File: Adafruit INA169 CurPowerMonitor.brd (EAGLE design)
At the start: 22.9 x 21 mm, 13 parts, among them U1 INA169

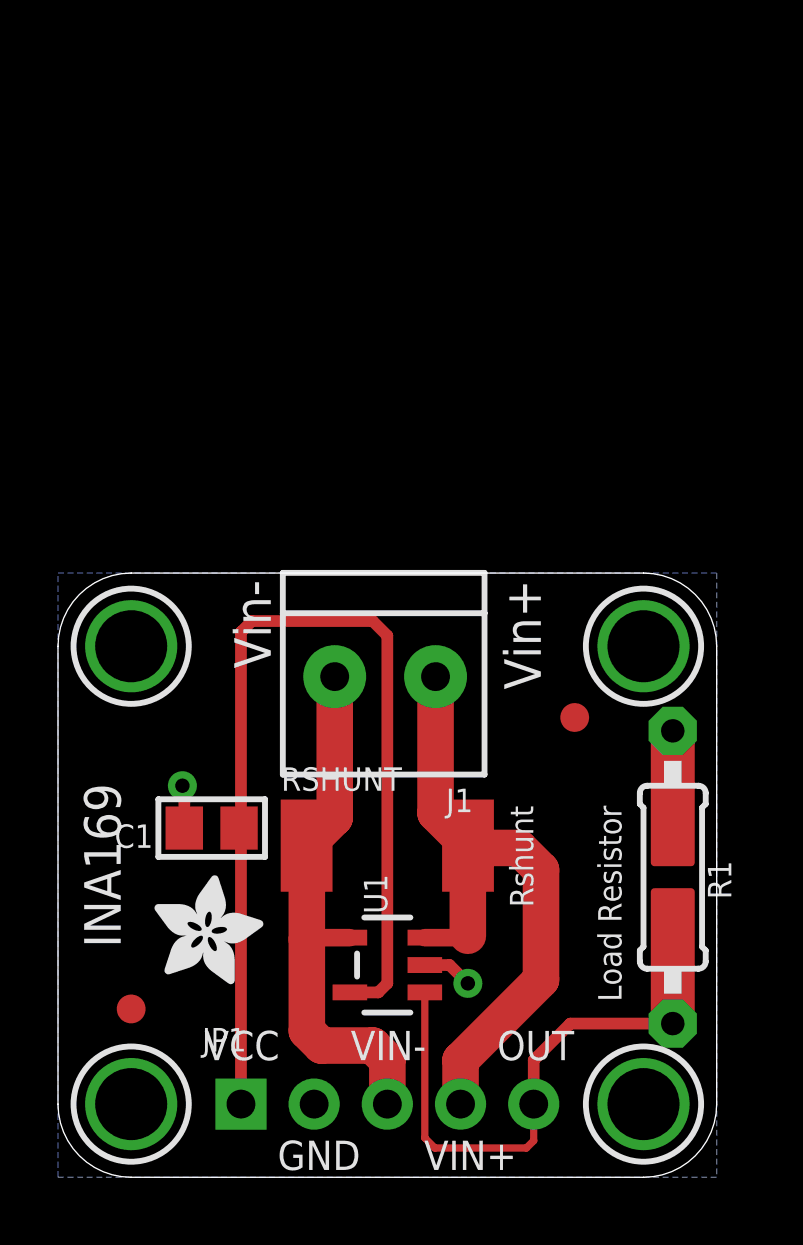
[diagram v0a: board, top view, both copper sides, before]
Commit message: add load switch and rework for 24p DIL 600mil outline
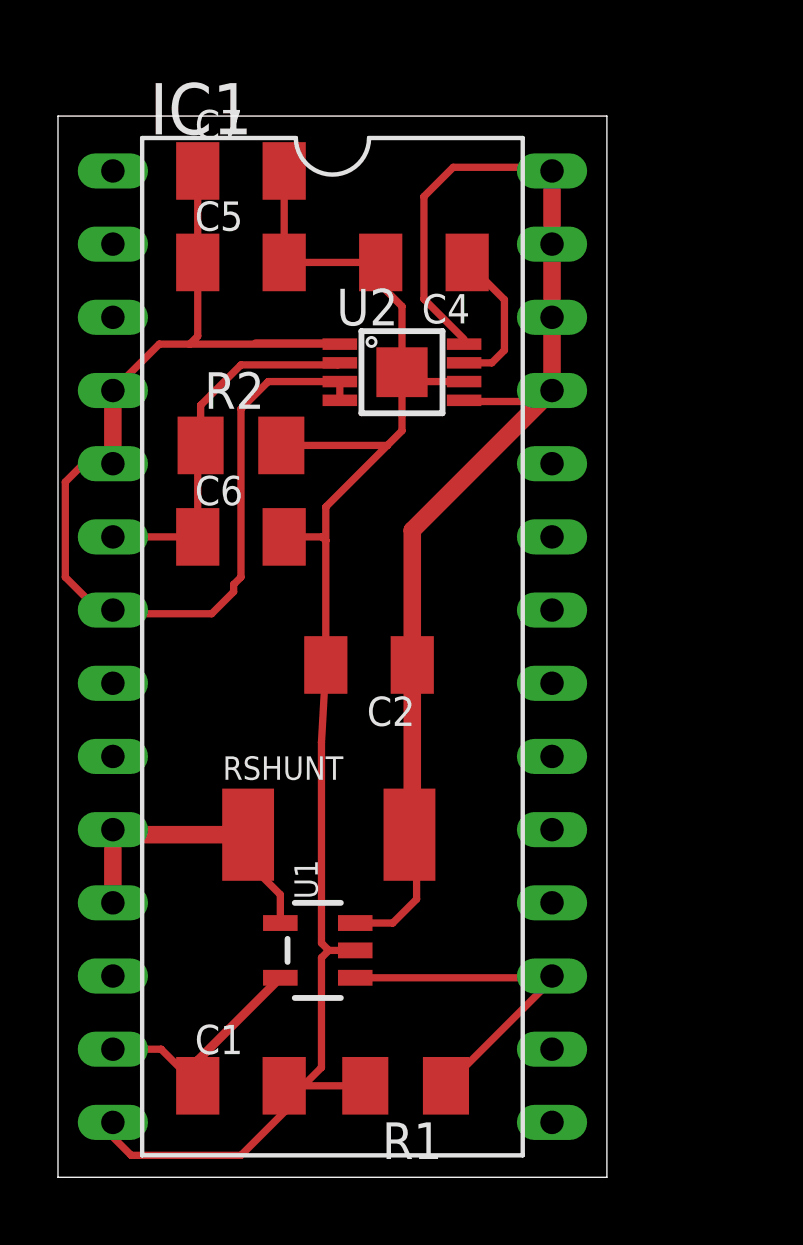
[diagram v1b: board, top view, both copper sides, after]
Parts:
- removed FID1, FID2: FIDUCIAL"", microbuilder:FIDUCIAL_1MM
- removed J1: (no value), microbuilder:TERMBLOCK_1X2-3.5MM
- removed JP1: (no value), microbuilder:1X05_ROUND_70
- removed U$10, U$7, U$8, U$9: MOUNTINGHOLE2.5, microbuilder:MOUNTINGHOLE_2.5_PLATED
- removed U$11: (no value), microbuilder:ADAFRUIT_3.5MM
- added C2: 0.1uF, resistor:C1206K
- added C4: 1000pF, resistor:C1206K
- added C5, C6: 0.01uF, resistor:C1206K
- added C7: 1uF, resistor:C1206K
- added IC1: board outline, ic-package:DIL28-6
- added R2: 10K, resistor:M1206
- added U2: TPS22958, worlickwerx:S-PDSO-G08
- C1: value 0.1µF -> 0.1uF; device microbuilder:0805 -> resistor:C1206K
- R1: device microbuilder:0805-THM -> resistor:M1206
- moved R1 11.8 mm to (12.1, 3.17), turned to 180 degrees
- moved C1 9.00 mm to (6.35, 3.17), turned to 0 degrees
- moved U1 2.47 mm to (9.02, 7.87)
- moved RSHUNT 2.07 mm to (9.40, 11.9)
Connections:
- removed net OUT: JP1.5, R1.1, U1.1
- removed net VIN+: J1.2, JP1.4, RSHUNT.2, U1.3
- removed net VIN-: J1.1, JP1.3, RSHUNT.1, U1.4
- new net CT: C4.1, U2.7
- new net PWR-MEAS: IC1.17, R1.1, U1.1
- new net PWR-ON: C6.1, IC1.6, R2.1, U2.2
- new net SWITCHED: C2.1, IC1.25, IC1.26, IC1.27, IC1.28, RSHUNT.2, U1.3, U2.5, U2.8
- new net VIN: C5.1, C7.1, IC1.4, IC1.5, IC1.7, U2.1, U2.3, U2.4
- new net VOUT: IC1.10, IC1.11, RSHUNT.1, U1.4
- net GND: now also C2.2, C4.2, C5.2, C6.2, C7.2, IC1.14, R2.2, U2.6; no longer JP1.2
- net VCC: now also IC1.13; no longer JP1.1
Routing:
- net GND: track 3.64 -> 56.7 mm, vias 2 -> 0
- net VIN: track 0.00 -> 43.1 mm
- net SWITCHED: track 0.00 -> 42.9 mm
- net VCC: track 35.4 -> 8.41 mm
- net VIN+: track 23.2 -> 0.00 mm
- net VIN-: track 18.9 -> 0.00 mm
- net OUT: track 17.2 -> 0.00 mm
- net PWR-ON: track 0.00 -> 13.0 mm
- net PWR-MEAS: track 0.00 -> 12.2 mm
- net VOUT: track 0.00 -> 9.98 mm
- net CT: track 0.00 -> 5.16 mm
- removed copper zone on layer 16, net GND
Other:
- board size 22.9 x 21 mm -> 19.1 x 36.8 mm
- board text removed: "GND"
- board text removed: "INA169"
- board text removed: "Load Resistor"
- board text removed: "OUT"
- board text removed: "Rshunt"
- board text removed: "VCC"
- board text removed: "VIN+"
- board text removed: "VIN-"
- board text removed: "Vin+"
- board text removed: "Vin-"
